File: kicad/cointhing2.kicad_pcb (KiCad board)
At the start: 2 copper layers, 35 x 34 mm, 29 parts, among them J1 USB_B_Micro, Q1 BC847BS, Q2 S8050_J3Y, U1 CP2102-GMR_NRND, U2 ESP-12E, U3 AMS1117-3.3

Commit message: PCB update
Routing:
- net /~{Reset}: track 45.9 -> 34.5 mm
- net /RTS: track 45.4 -> 35.0 mm
- net Net-(R4-Pad2): track 33.7 -> 26.9 mm, vias 0 -> 2
- net Net-(R3-Pad2): track 16.8 -> 11.5 mm
- net +3V3: track 61.6 -> 66.1 mm
- net /LEDA: track 7.42 -> 11.4 mm
- net /GPIO0: track 41.5 -> 45.3 mm
- net /LEDK: track 12.7 -> 9.08 mm
- net Net-(R1-Pad1): track 22.7 -> 19.2 mm
- net /TFT_BL: track 32.1 -> 35.5 mm, vias 2 -> 0
- net /DTR: track 40.4 -> 37.9 mm
- net /D+: track 10.4 -> 8.35 mm
- net /TFT_SCL: track 7.19 -> 9.23 mm
- net VBUS: track 55.9 -> 57.2 mm
- net /D-: track 10.00 -> 8.74 mm
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
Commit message: PCB rev.B ready
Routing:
- net /~{Reset}: track 34.5 -> 35.5 mm
- net Net-(R4-Pad2): track 26.9 -> 27.5 mm
- net GND: vias 4 -> 5

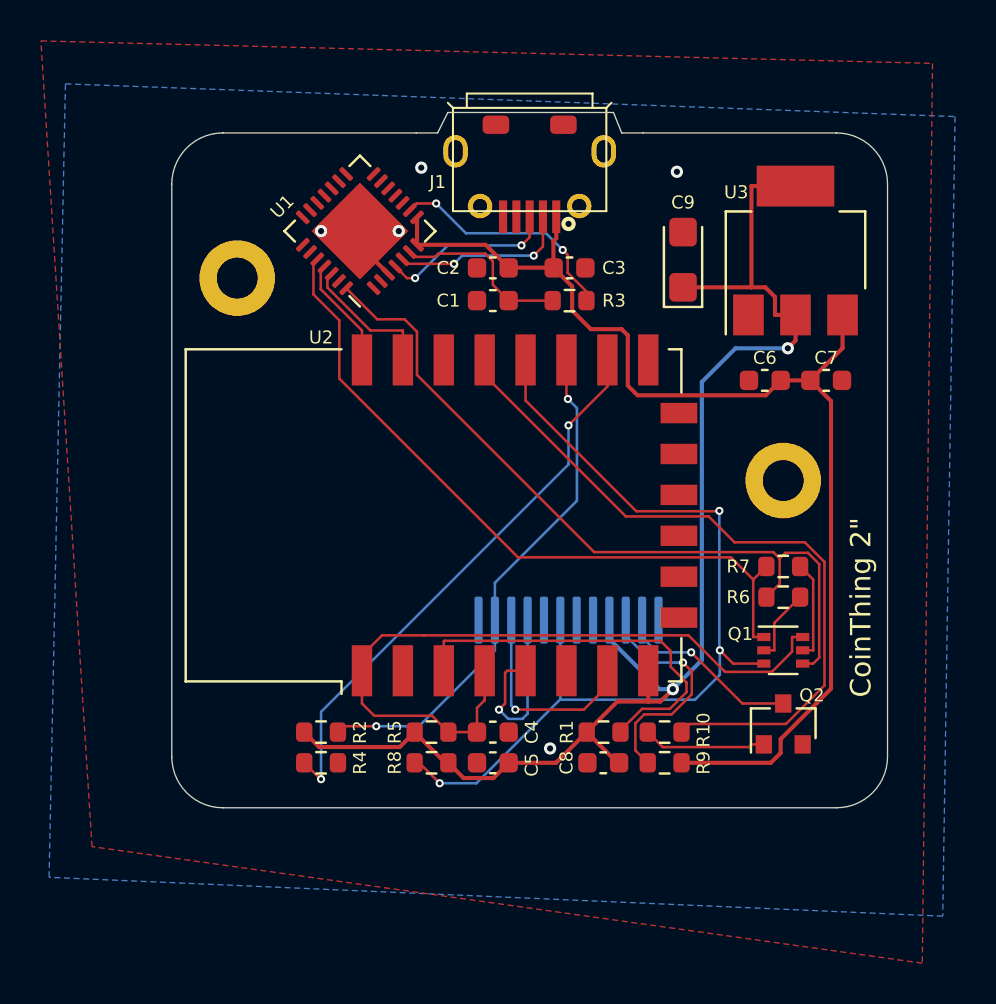
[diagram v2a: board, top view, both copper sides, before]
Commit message: Schematic: new diode from GPIO16 to RESET
In order for the deep sleep wake up will work with the auto programming circuit
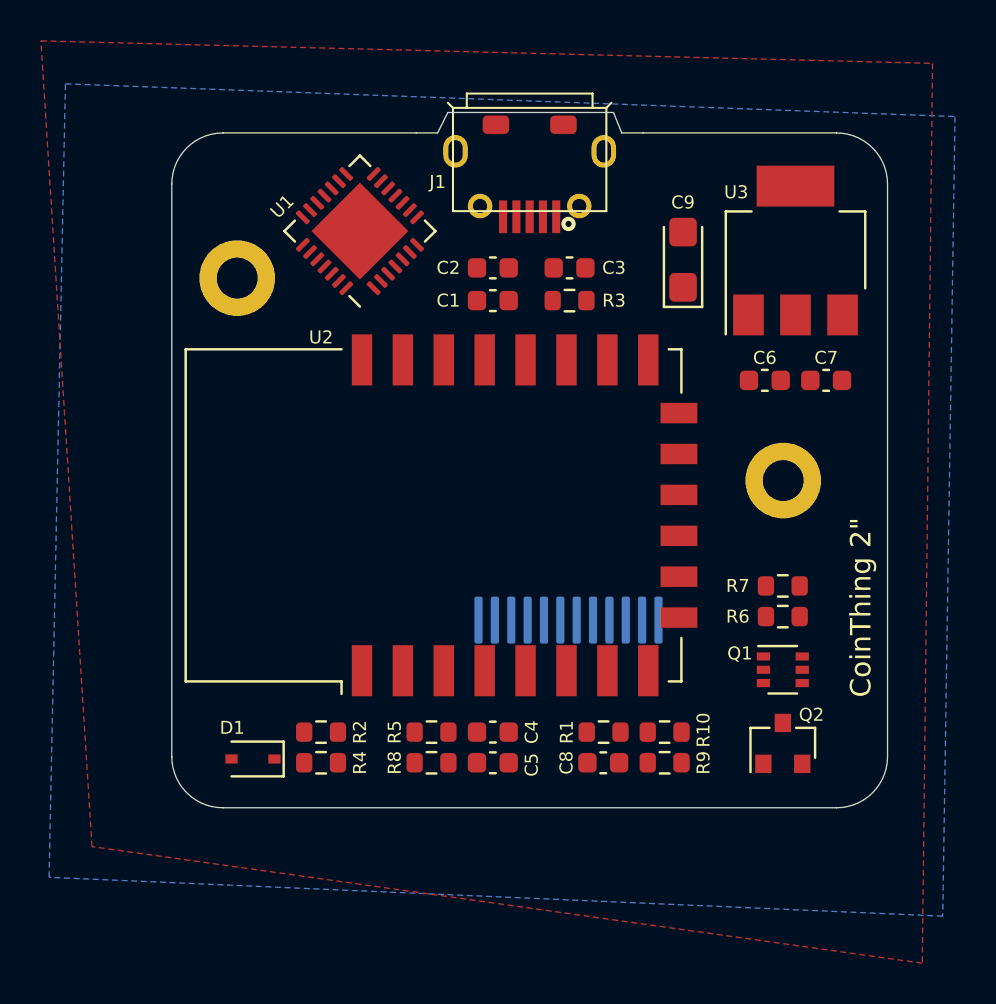
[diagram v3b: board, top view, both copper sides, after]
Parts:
- added D1: BAS321,115, Diode_SMD:D_SOD-323, F.Cu at (149.0, 86.6)
- moved Q1 0.95 mm to (174.9, 82.3)
- moved Q2 0.95 mm to (174.9, 85.9)
- moved R6 0.95 mm to (174.9, 79.7)
- moved R7 0.95 mm to (174.9, 78.2)
- renumbered D1 to LCD1
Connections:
- U2 pad 4: /~{Reset} -> Net-(U2-Pad4)
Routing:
- net +3V3: track 66.1 -> 0.00 mm, vias 2 -> 0
- net VBUS: track 57.2 -> 0.00 mm
- net /GPIO0: track 45.6 -> 0.00 mm, vias 3 -> 0
- net /DTR: track 37.9 -> 0.00 mm
- net /~{Reset}: track 35.5 -> 0.00 mm
- net /TFT_BL: track 35.1 -> 0.00 mm
- net /RTS: track 35.0 -> 0.00 mm
- net Net-(R4-Pad2): track 27.5 -> 0.00 mm, vias 2 -> 0
- net /~{TFT_RES}: track 25.4 -> 0.00 mm, vias 2 -> 0
- net Net-(R1-Pad1): track 19.2 -> 0.00 mm
- net Net-(R3-Pad2): track 11.5 -> 0.00 mm, vias 2 -> 0
- net /LEDA: track 11.4 -> 0.00 mm, vias 1 -> 0
- net /TFT_SDA: track 10.2 -> 0.00 mm, vias 1 -> 0
- net /TFT_SCL: track 9.23 -> 0.00 mm, vias 1 -> 0
- net /LEDK: track 9.08 -> 0.00 mm, vias 1 -> 0
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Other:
- board text added: "CoinThing 2{dblquote} barn53 rev.C 11/22"
- board text removed: "CoinThing 2{dblquote} barn53 rev.B 02/22"
